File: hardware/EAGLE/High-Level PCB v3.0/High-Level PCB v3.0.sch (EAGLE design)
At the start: 31 parts, among them IC1 DS8921, IC2 DS8921, J1 Micro-SD, J2 Gyro, J3 Compass, J4 GPS, J5 CAN BUS, J6 Compass, X1 RJ45, X2 Vehicle control, X4 RJ45

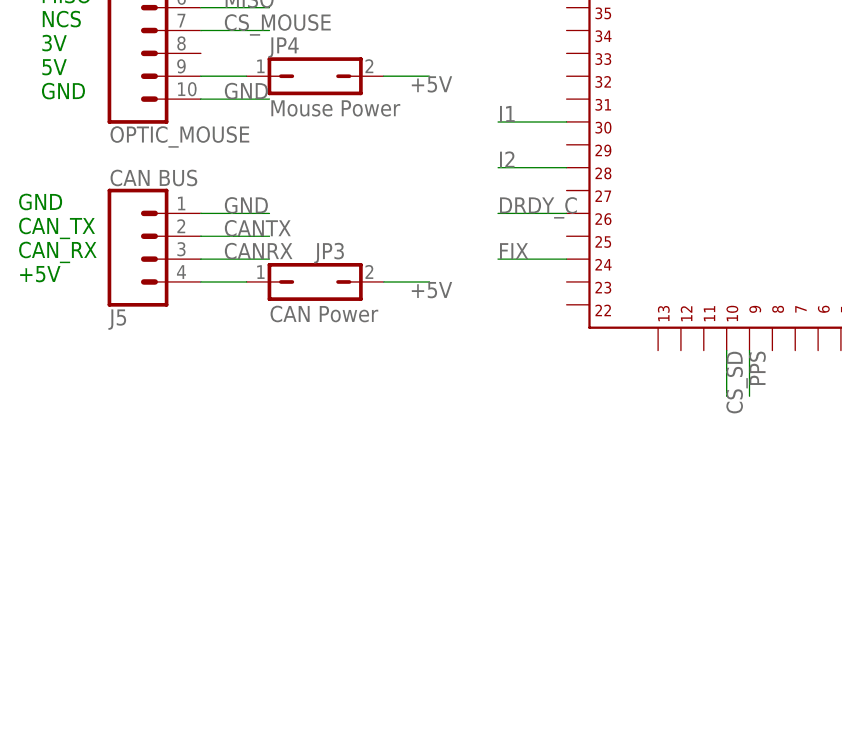
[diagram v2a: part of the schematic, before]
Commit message: Added CAN bus chip (MCP2551)
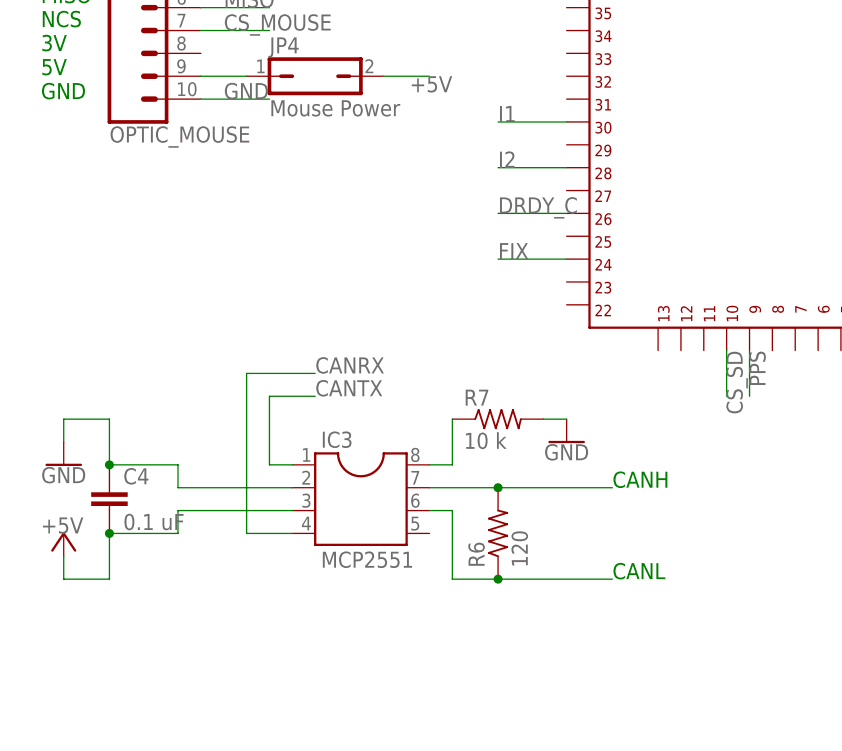
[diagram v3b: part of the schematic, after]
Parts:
- removed J5: CAN BUS, SparkFun-Connectors:CONN_04
- removed JP3: CAN Power, jumper:JP1Q
- added C4: 0.1 uF, capacitor-wima:C2.5/5
- added IC3: MCP2551, ic-package:DIL8
- added R6: 120, rcl:R-US_0204/5
- added R7: 10 k, rcl:R-US_0204/5
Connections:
- removed net N$11: J5.4, JP3.1
- new net N$15: IC3.7, R6.2
- new net N$16: IC3.6, R6.1
- new net N$17: IC3.8, R7.1
- net +5V: now also C4.2, IC3.3; no longer JP3.2
- net CANRX: now also IC3.4; no longer J5.3
- net CANTX: now also IC3.1; no longer J5.2
- net GND: now also C4.1, IC3.2, R7.2; no longer J5.1
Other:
- note added: "CANH"
- note added: "CANL"
- note removed: "GND CAN_TX CAN_RX +5V"
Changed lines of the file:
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@@
 <part name="P+2" library="supply1" library_urn="urn:adsk.eagle:library:371" deviceset="+5V" device=""/>
 <part name="P+3" library="supply1" library_urn="urn:adsk.eagle:library:371" deviceset="+5V" device=""/>
-<part name="J5" library="SparkFun-Connectors" library_urn="urn:adsk.eagle:library:513" deviceset="CONN_04" device="" package3d_urn="urn:adsk.eagle:package:38085/1" value="CAN BUS"/>
 <part name="B1" library="SparkFun-Boards" deviceset="SPARKFUN_LOGIC_LEVEL_CONVERTER" device=""/>
 <part name="GND7" library="SparkFun-PowerSymbols" deviceset="GND" device=""/>
@@
 <part name="JP7" library="jumper" library_urn="urn:adsk.eagle:library:252" deviceset="JP1Q" device="" package3d_urn="urn:adsk.eagle:package:15455/1" value="Gyro Power"/>
 <part name="JP1" library="jumper" library_urn="urn:adsk.eagle:library:252" deviceset="JP1Q" device="" package3d_urn="urn:adsk.eagle:package:15455/1" value="MicroSD Power"/>
-<part name="JP3" library="jumper" library_urn="urn:adsk.eagle:library:252" deviceset="JP1Q" device="" package3d_urn="urn:adsk.eagle:package:15455/1" value="CAN Power"/>
 <part name="JP4" library="jumper" library_urn="urn:adsk.eagle:library:252" deviceset="JP1Q" device="" package3d_urn="urn:adsk.eagle:package:15455/1" value="Mouse Power"/>
 <part name="JP5" library="jumper" library_urn="urn:adsk.eagle:library:252" deviceset="JP1Q" device="" package3d_urn="urn:adsk.eagle:package:15455/1" value="GPS Power"/>
@@
 <part name="P+4" library="supply1" library_urn="urn:adsk.eagle:library:371" deviceset="+5V" device=""/>
 <part name="P+6" library="supply1" library_urn="urn:adsk.eagle:library:371" deviceset="+5V" device=""/>
+<part name="IC3" library="ic-package" library_urn="urn:adsk.eagle:library:239" deviceset="DIL8" device="" package3d_urn="urn:adsk.eagle:package:14440/1" value="MCP2551"/>
+<part name="R6" library="rcl" library_urn="urn:adsk.eagle:library:334" deviceset="R-US_" device="0204/5" package3d_urn="urn:adsk.eagle:package:23488/1" value="120"/>
+<part name="R7" library="rcl" library_urn="urn:adsk.eagle:library:334" deviceset="R-US_" device="0204/5" package3d_urn="urn:adsk.eagle:package:23488/1" value="10 k"/>
+<part name="P+5" library="supply1" library_urn="urn:adsk.eagle:library:371" deviceset="+5V" device=""/>
+<part name="GND8" library="SparkFun-PowerSymbols" deviceset="GND" device=""/>
+<part name="C4" library="capacitor-wima" library_urn="urn:adsk.eagle:library:116" deviceset="C" device="2.5/5" package3d_urn="urn:adsk.eagle:package:5407/1" value="0.1 uF"/>
+<part name="GND9" library="SparkFun-PowerSymbols" deviceset="GND" device=""/>
 </parts>
 <sheets>
@@
 5V
 GND</text>
-<text x="10.16" y="60.96" size="1.778" layer="91">GND
-CAN_TX
-CAN_RX
-+5V</text>
+<text x="76.2" y="38.1" size="1.778" layer="91">CANH</text>
+<text x="76.2" y="27.94" size="1.778" layer="91">CANL</text>
 </plain>
 <instances>
@@
 <instance part="P+2" gate="1" x="185.42" y="200.66"/>
 <instance part="P+3" gate="1" x="185.42" y="167.64"/>
-<instance part="J5" gate="G$1" x="25.4" y="66.04" rot="MR180"/>
 <instance part="B1" gate="G$1" x="139.7" y="20.32" smashed="yes">
 <attribute name="NAME" x="134.62" y="30.734" size="1.778" layer="95" font="vector"/>
@@
 <instance part="JP7" gate="A" x="187.96" y="88.9" rot="R90"/>
 <instance part="JP1" gate="A" x="187.96" y="78.74" rot="R90"/>
-<instance part="JP3" gate="A" x="43.18" y="60.96" smashed="yes" rot="R270">
-<attribute name="NAME" x="43.18" y="63.5" size="1.778" layer="95"/>
-<attribute name="VALUE" x="38.1" y="56.515" size="1.778" layer="96"/>
-</instance>
 <instance part="JP4" gate="A" x="43.18" y="83.82" rot="R270"/>
 <instance part="JP5" gate="A" x="43.18" y="116.84" smashed="yes" rot="R270">
@@
 <attribute name="VALUE" x="139.7" y="53.34" size="1.778" layer="96"/>
 </instance>
+<instance part="IC3" gate="G$1" x="48.26" y="38.1"/>
+<instance part="R6" gate="G$1" x="63.5" y="33.02" rot="R90"/>
+<instance part="R7" gate="G$1" x="63.5" y="45.72"/>
+<instance part="P+5" gate="1" x="15.24" y="33.02" smashed="yes">
+<attribute name="VALUE" x="12.7" y="33.02" size="1.778" layer="96"/>
+</instance>
+<instance part="GND8" gate="1" x="15.24" y="40.64"/>
+<instance part="C4" gate="G$1" x="20.32" y="38.1"/>
+<instance part="GND9" gate="1" x="71.12" y="43.18"/>
 </instances>
 <busses>
@@
 <pinref part="X1" gate="G$1" pin="1"/>
 <wire x1="243.84" y1="180.34" x2="251.46" y2="180.34" width="0.1524" layer="91"/>
-</segment>
-<segment>
-<pinref part="J5" gate="G$1" pin="1"/>
-<wire x1="30.48" y1="68.58" x2="38.1" y2="68.58" width="0.1524" layer="91"/>
-<label x="33.02" y="68.58" size="1.778" layer="95"/>
 </segment>
 <segment>
@@
 <pinref part="GND7" gate="1" pin="GND"/>
 <junction x="137.16" y="7.62"/>
+</segment>
+<segment>
+<pinref part="GND8" gate="1" pin="GND"/>
+<wire x1="15.24" y1="45.72" x2="15.24" y2="43.18" width="0.1524" layer="91"/>
+<pinref part="IC3" gate="G$1" pin="2"/>
+<wire x1="40.64" y1="38.1" x2="27.94" y2="38.1" width="0.1524" layer="91"/>
+<wire x1="27.94" y1="38.1" x2="27.94" y2="40.64" width="0.1524" layer="91"/>
+<pinref part="C4" gate="G$1" pin="1"/>
+<wire x1="27.94" y1="40.64" x2="20.32" y2="40.64" width="0.1524" layer="91"/>
+<wire x1="20.32" y1="40.64" x2="20.32" y2="45.72" width="0.1524" layer="91"/>
+<junction x="20.32" y="40.64"/>
+<wire x1="20.32" y1="45.72" x2="15.24" y2="45.72" width="0.1524" layer="91"/>
+</segment>
+<segment>
+<pinref part="GND9" gate="1" pin="GND"/>
+<pinref part="R7" gate="G$1" pin="2"/>
+<wire x1="71.12" y1="45.72" x2="68.58" y2="45.72" width="0.1524" layer="91"/>
 </segment>
 </net>
@@
 </segment>
 <segment>
-<pinref part="JP3" gate="A" pin="2"/>
-<wire x1="50.8" y1="60.96" x2="55.88" y2="60.96" width="0.1524" layer="91"/>
-<label x="58.42" y="60.96" size="1.778" layer="95" rot="R180"/>
-</segment>
-<segment>
 <pinref part="JP4" gate="A" pin="2"/>
 <wire x1="50.8" y1="83.82" x2="55.88" y2="83.82" width="0.1524" layer="91"/>
@@
 <pinref part="R5" gate="G$1" pin="1"/>
 <pinref part="P+6" gate="1" pin="+5V"/>
+</segment>
+<segment>
+<pinref part="P+5" gate="1" pin="+5V"/>
+<wire x1="15.24" y1="30.48" x2="15.24" y2="27.94" width="0.1524" layer="91"/>
+<pinref part="IC3" gate="G$1" pin="3"/>
+<wire x1="40.64" y1="35.56" x2="27.94" y2="35.56" width="0.1524" layer="91"/>
+<pinref part="C4" gate="G$1" pin="2"/>
+<wire x1="27.94" y1="35.56" x2="27.94" y2="33.02" width="0.1524" layer="91"/>
+<wire x1="27.94" y1="33.02" x2="20.32" y2="33.02" width="0.1524" layer="91"/>
+<wire x1="20.32" y1="33.02" x2="20.32" y2="27.94" width="0.1524" layer="91"/>
+<junction x="20.32" y="33.02"/>
+<wire x1="15.24" y1="27.94" x2="20.32" y2="27.94" width="0.1524" layer="91"/>
 </segment>
 </net>
@@
 </segment>
 <segment>
-<pinref part="J5" gate="G$1" pin="3"/>
-<wire x1="30.48" y1="63.5" x2="38.1" y2="63.5" width="0.1524" layer="91"/>
-<label x="33.02" y="63.5" size="1.778" layer="95"/>
+<pinref part="IC3" gate="G$1" pin="4"/>
+<wire x1="40.64" y1="33.02" x2="35.56" y2="33.02" width="0.1524" layer="91"/>
+<wire x1="35.56" y1="33.02" x2="35.56" y2="50.8" width="0.1524" layer="91"/>
+<wire x1="35.56" y1="50.8" x2="43.18" y2="50.8" width="0.1524" layer="91"/>
+<label x="43.18" y="50.8" size="1.778" layer="95"/>
 </segment>
 </net>
@@
 </segment>
 <segment>
-<pinref part="J5" gate="G$1" pin="2"/>
-<wire x1="30.48" y1="66.04" x2="38.1" y2="66.04" width="0.1524" layer="91"/>
-<label x="33.02" y="66.04" size="1.778" layer="95"/>
+<pinref part="IC3" gate="G$1" pin="1"/>
+<wire x1="40.64" y1="40.64" x2="38.1" y2="40.64" width="0.1524" layer="91"/>
+<wire x1="38.1" y1="40.64" x2="38.1" y2="48.26" width="0.1524" layer="91"/>
+<wire x1="38.1" y1="48.26" x2="43.18" y2="48.26" width="0.1524" layer="91"/>
+<label x="43.18" y="48.26" size="1.778" layer="95"/>
 </segment>
 </net>
@@
 </segment>
 </net>
-<net name="N$11" class="0">
-<segment>
-<pinref part="J5" gate="G$1" pin="4"/>
-<pinref part="JP3" gate="A" pin="1"/>
-<wire x1="30.48" y1="60.96" x2="35.56" y2="60.96" width="0.1524" layer="91"/>
-</segment>
-</net>
 <net name="N$13" class="0">
 <segment>
@@
 </segment>
 </net>
+<net name="N$15" class="0">
+<segment>
+<pinref part="IC3" gate="G$1" pin="7"/>
+<pinref part="R6" gate="G$1" pin="2"/>
+<wire x1="55.88" y1="38.1" x2="63.5" y2="38.1" width="0.1524" layer="91"/>
+<wire x1="63.5" y1="38.1" x2="76.2" y2="38.1" width="0.1524" layer="91"/>
+<junction x="63.5" y="38.1"/>
+</segment>
+</net>
+<net name="N$16" class="0">
+<segment>
+<pinref part="R6" gate="G$1" pin="1"/>
+<wire x1="63.5" y1="27.94" x2="58.42" y2="27.94" width="0.1524" layer="91"/>
+<wire x1="58.42" y1="27.94" x2="58.42" y2="35.56" width="0.1524" layer="91"/>
+<pinref part="IC3" gate="G$1" pin="6"/>
+<wire x1="58.42" y1="35.56" x2="55.88" y2="35.56" width="0.1524" layer="91"/>
+<wire x1="63.5" y1="27.94" x2="76.2" y2="27.94" width="0.1524" layer="91"/>
+<junction x="63.5" y="27.94"/>
+</segment>
+</net>
+<net name="N$17" class="0">
+<segment>
+<pinref part="R7" gate="G$1" pin="1"/>
+<wire x1="58.42" y1="45.72" x2="58.42" y2="40.64" width="0.1524" layer="91"/>
+<pinref part="IC3" gate="G$1" pin="8"/>
+<wire x1="58.42" y1="40.64" x2="55.88" y2="40.64" width="0.1524" layer="91"/>
+</segment>
+</net>

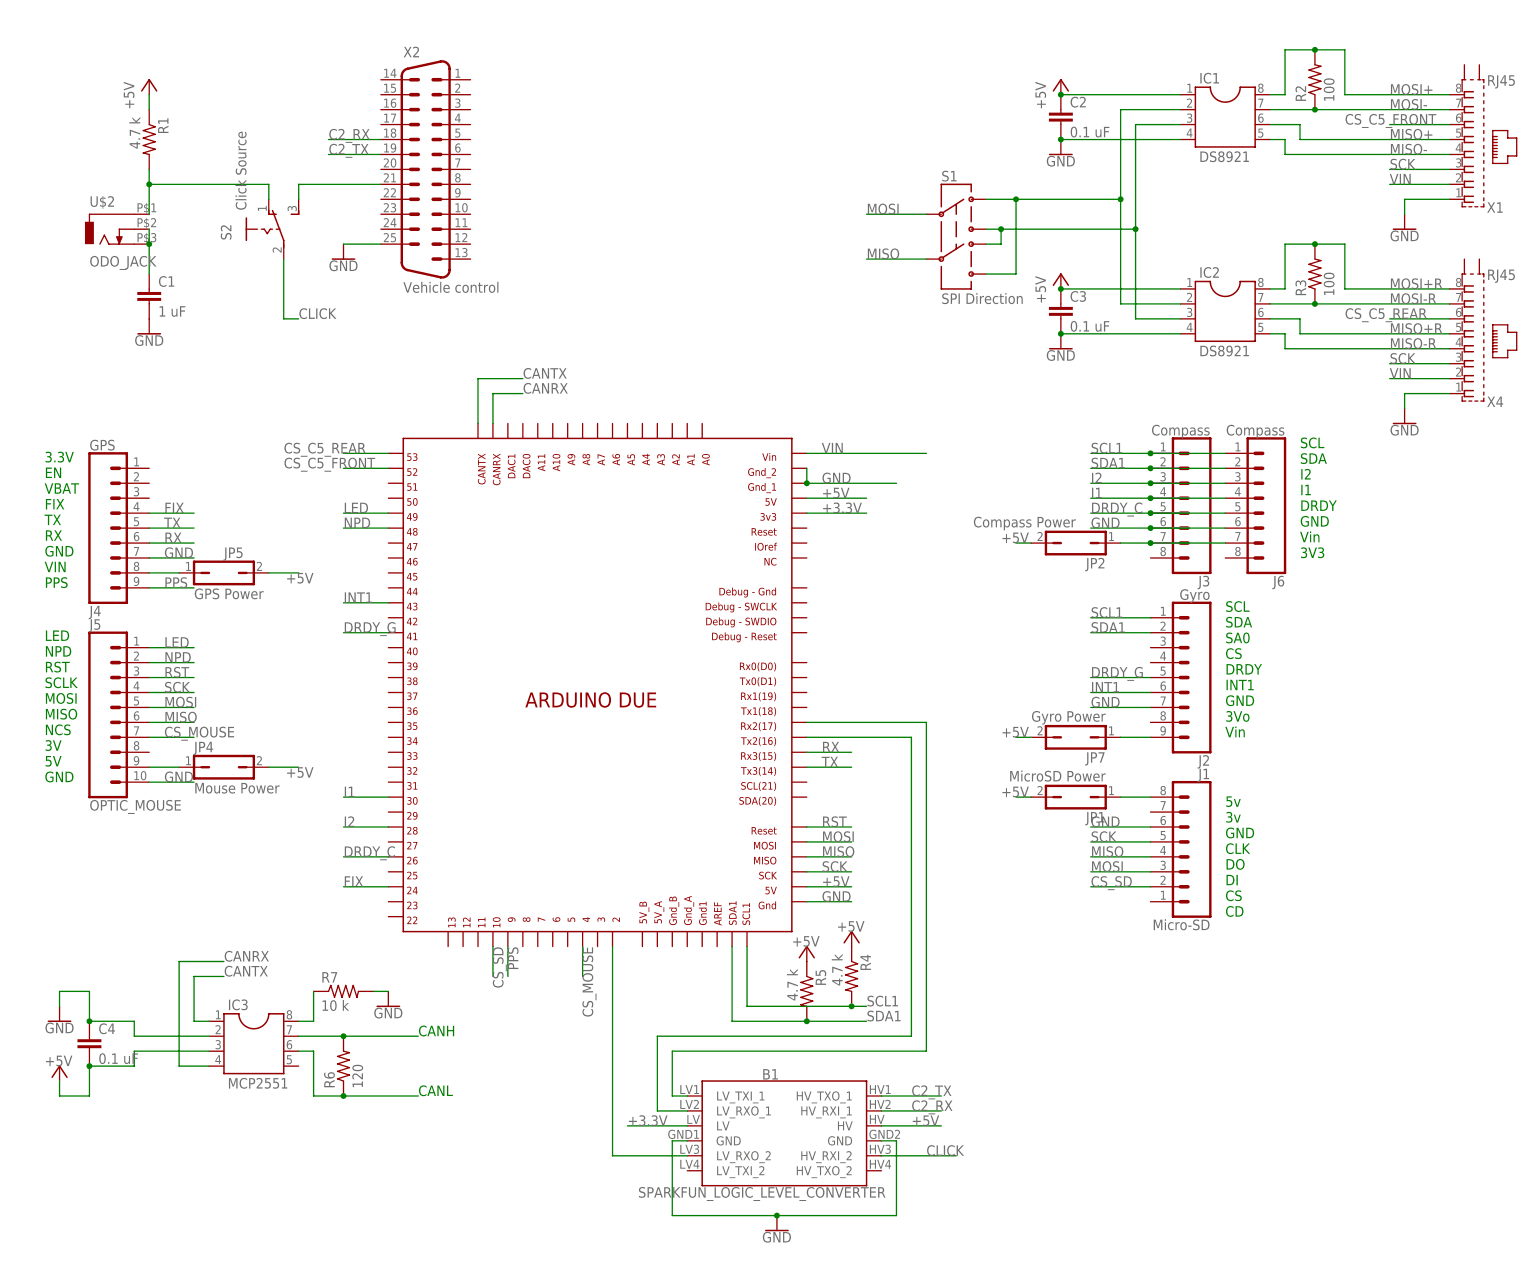
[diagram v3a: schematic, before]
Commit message: Added DB9 and terminal block connectors
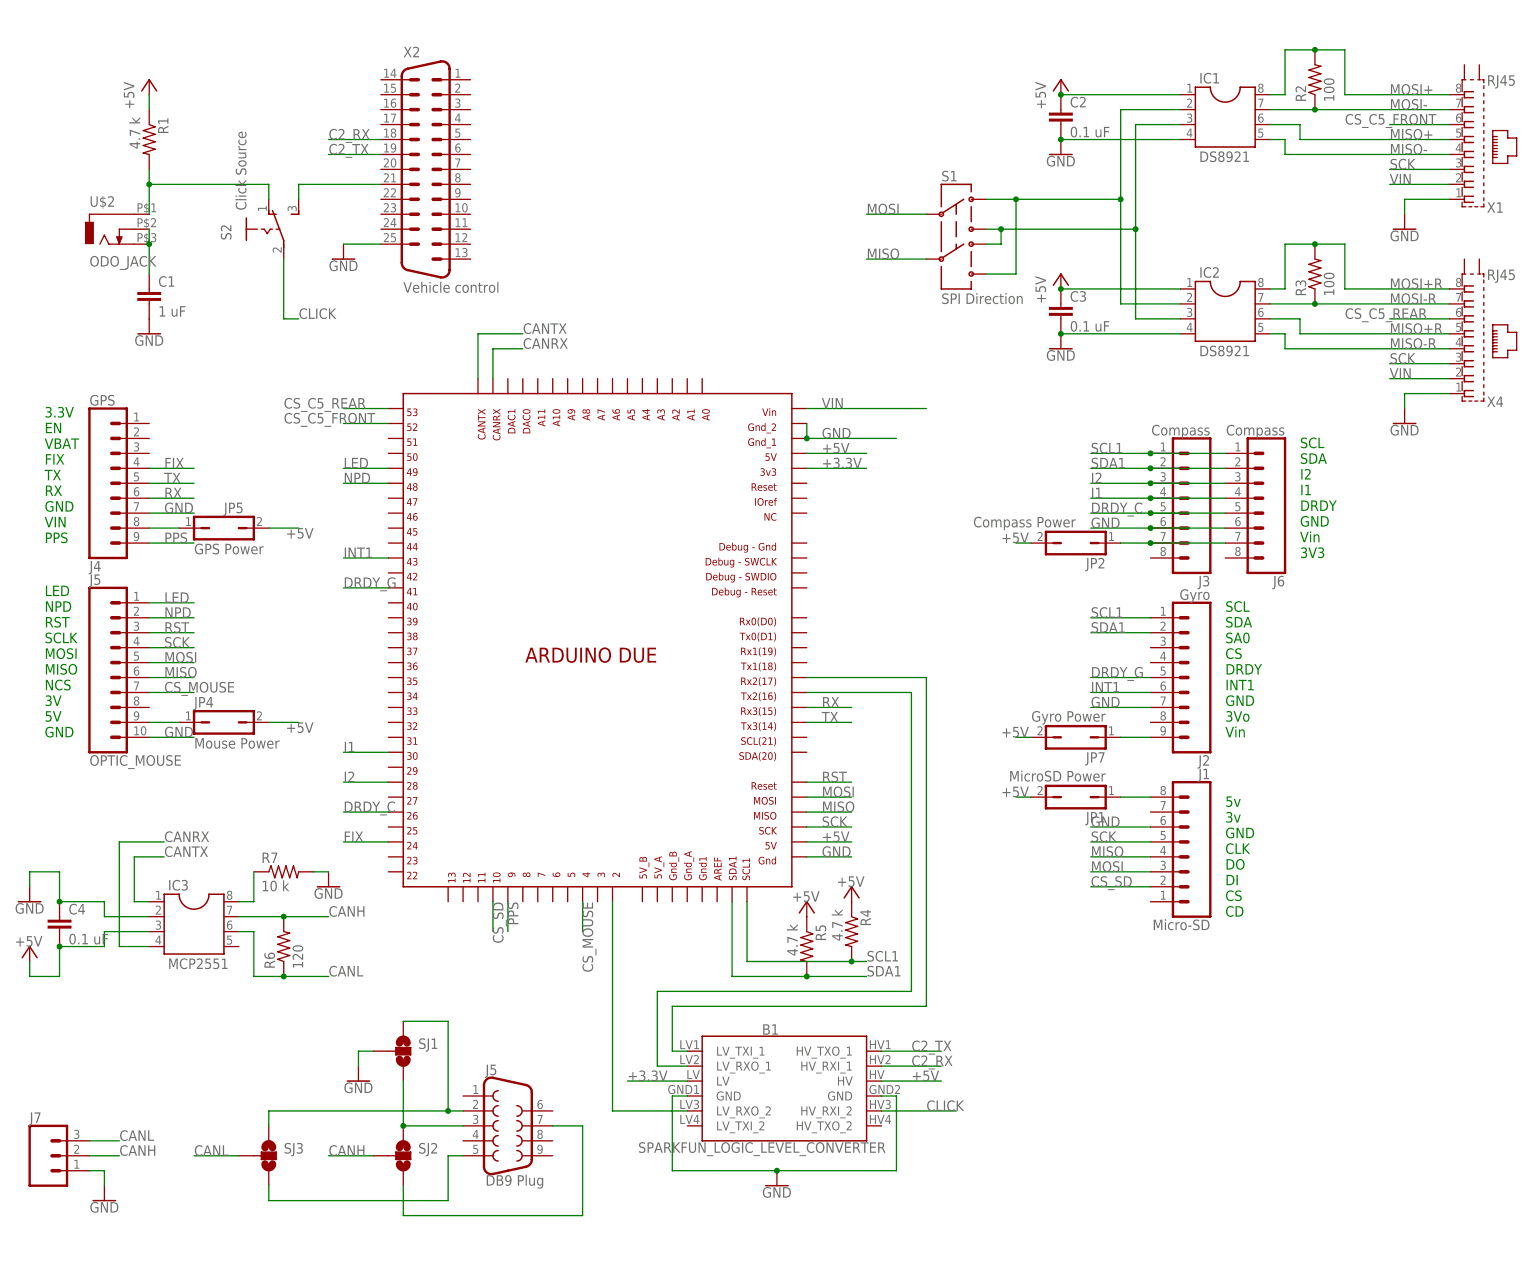
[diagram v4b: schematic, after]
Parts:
- added J5: DB9 Plug, SparkFun-Connectors:DB9MALE
- added J7: (no value), SparkFun-Connectors:CONN_03-SCREW-5MM
- added SJ1, SJ2, SJ3: JUMPER-SMT_3_NO_SILK, SparkFun-Jumpers:JUMPER-SMT_3_NO_SILK
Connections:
- new net CANH: IC3.7, J7.2, R6.2, SJ2.2
- new net CANL: IC3.6, J7.3, R6.1, SJ3.2
- new net N$11: J5.3, SJ1.3, SJ2.1
- new net N$18: J5.2, SJ1.1, SJ3.1
- net GND: now also J7.1, SJ1.2
- net N$15: now also J5.5, SJ3.3; no longer IC3.7, R6.2
- net N$16: now also J5.7, SJ2.3; no longer IC3.6, R6.1
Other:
- note removed: "CANH"
- note removed: "CANL"
- moved on the sheet: B1, C4, IC3, J4, JP4, JP5, OPTIC_MOUSE, R4, R5, R6, R7
